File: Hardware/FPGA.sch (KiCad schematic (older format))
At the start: 6 parts, among them U501 W25Q128JVxxM, U502 ICE40UP5K-SG48, U503 Crystal Oscillator, U504 USBLC6-2

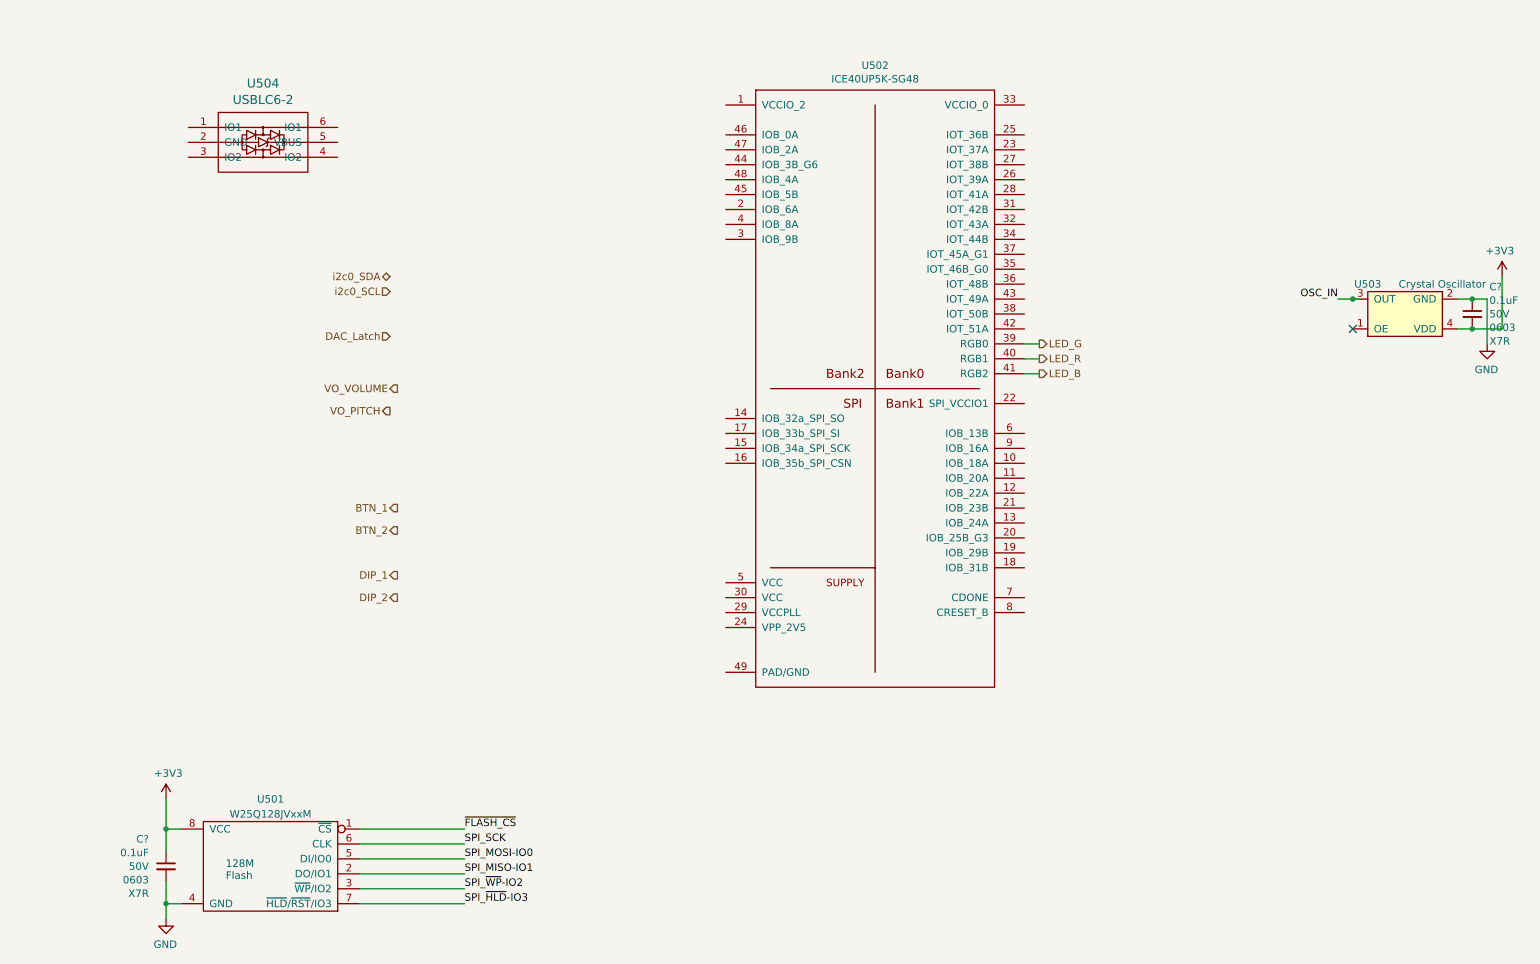
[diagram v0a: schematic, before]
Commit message: Putting in some connectivity. More passives.
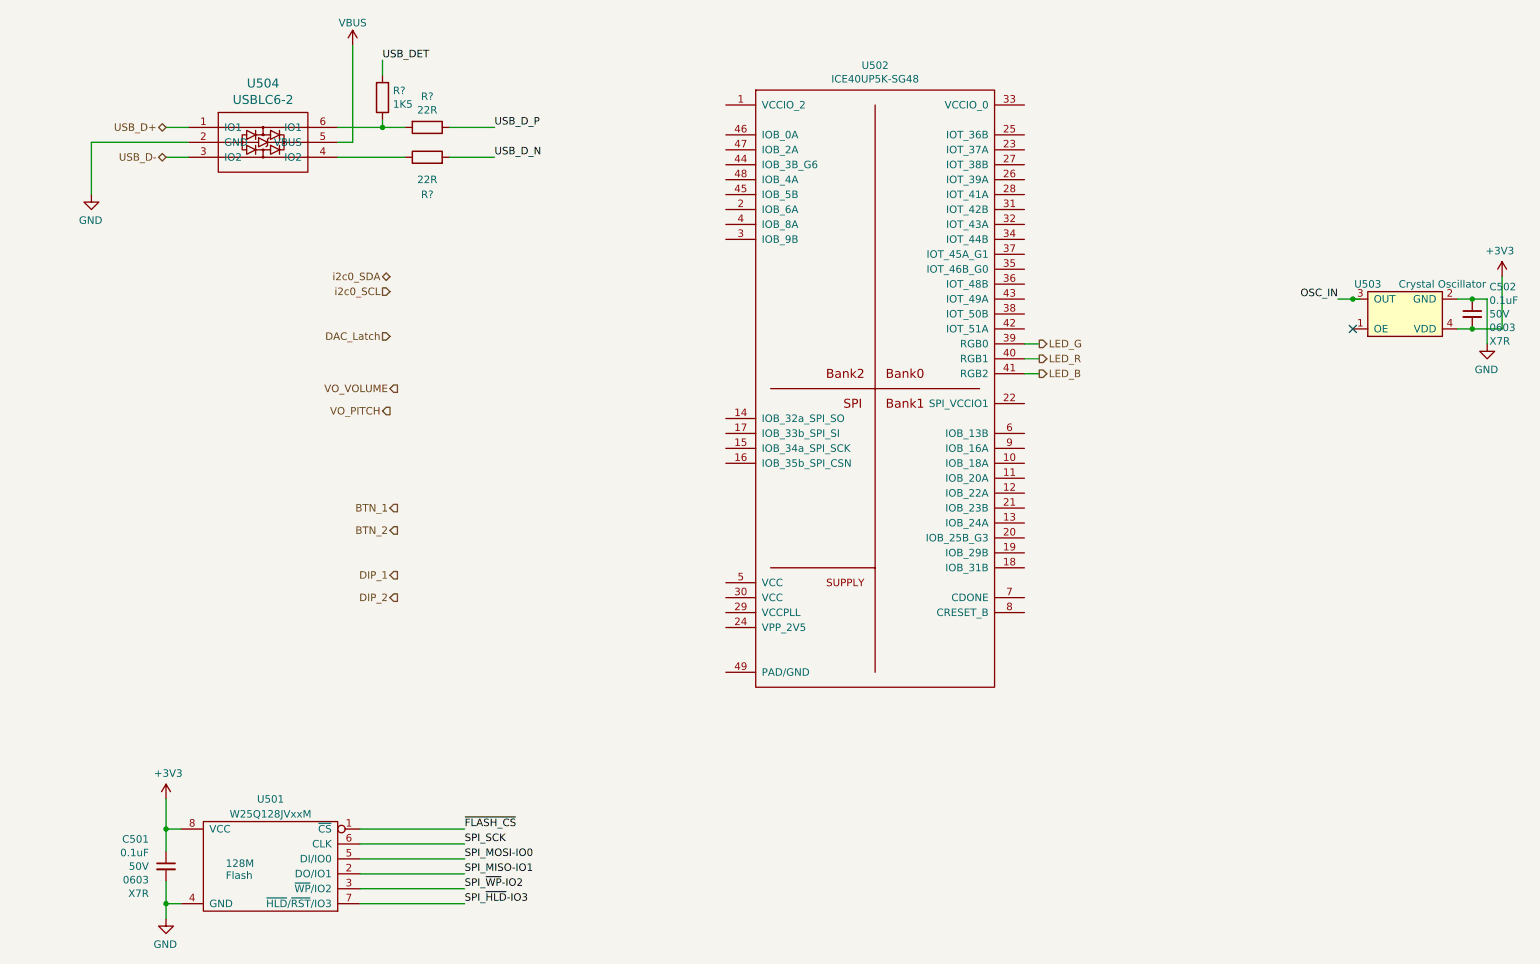
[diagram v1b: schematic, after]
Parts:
- added R? (x2): 22R, Resistor_SMD:R_0603_1608Metric, symbol Device:R
- added R?: 1K5, Resistor_SMD:R_0603_1608Metric, symbol Device:R
- gave numbers to parts that had none: 2
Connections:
- net labels added: USB_D+, USB_D-, USB_DET, USB_D_N, USB_D_P, VBUS
- wire segments 23 -> 36
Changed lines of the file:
@@
 P 10450 2650
 AR Path="/611E335F/61350B96" Ref="C?"  Part="1"
-AR Path="/611E3335/61350B96" Ref="C?"  Part="1"
-F 0 "C?" H 10565 2832 50  0000 L CNN
+AR Path="/611E3335/61350B96" Ref="C502"  Part="1"
+F 0 "C502" H 10565 2832 50  0000 L CNN
 F 1 "0.1uF" H 10565 2741 50  0000 L CNN
 F 2 "Capacitor_SMD:C_0603_1608Metric" H 10488 2500 50  0001 C CNN
@@
 	10450 2750 10650 2750
 $Comp
-L power:GND #PWR?
+L power:GND #PWR0108
 U 1 1 613565CE
 P 1700 6700
-F 0 "#PWR?" H 1700 6450 50  0001 C CNN
+F 0 "#PWR0108" H 1700 6450 50  0001 C CNN
 F 1 "GND" H 1705 6527 50  0000 C CNN
 F 2 "" H 1700 6700 50  0001 C CNN
@@
 	1700 5900 1700 6100
 $Comp
-L power:+3V3 #PWR?
+L power:+3V3 #PWR0109
 U 1 1 6135A9D4
 P 1700 5900
-F 0 "#PWR?" H 1700 5750 50  0001 C CNN
+F 0 "#PWR0109" H 1700 5750 50  0001 C CNN
 F 1 "+3V3" H 1715 6073 50  0000 C CNN
 F 2 "" H 1700 5900 50  0001 C CNN
@@
 P 1700 6350
 AR Path="/611E335F/6135A9DF" Ref="C?"  Part="1"
-AR Path="/611E3335/6135A9DF" Ref="C?"  Part="1"
-F 0 "C?" H 1815 6532 50  0000 L CNN
+AR Path="/611E3335/6135A9DF" Ref="C501"  Part="1"
+F 0 "C501" H 1815 6532 50  0000 L CNN
 F 1 "0.1uF" H 1815 6441 50  0000 L CNN
 F 2 "Capacitor_SMD:C_0603_1608Metric" H 1738 6200 50  0001 C CNN
@@
 Wire Wire Line
 	1700 6600 1800 6600
+$Comp
+L Device:R R?
+U 1 1 61492D03
+P 3450 1400
+AR Path="/61492D03" Ref="R?"  Part="1"
+AR Path="/611E3335/61492D03" Ref="R?"  Part="1"
+F 0 "R?" V 3243 1400 50  0000 C CNN
+F 1 "22R" V 3334 1400 50  0000 C CNN
+F 2 "Resistor_SMD:R_0603_1608Metric" V 3380 1400 50  0001 C CNN
+F 3 "~" H 3450 1400 50  0001 C CNN
+F 4 "CRGCQ0603J22R" V 3450 1400 50  0001 C CNN "MPN"
+F 5 "A130081CT-ND" V 3450 1400 50  0001 C CNN "DPN"
+	1    3450 1400
+	0    1    1    0
+$EndComp
+$Comp
+L Device:R R?
+U 1 1 61492D0B
+P 3150 1200
+AR Path="/61492D0B" Ref="R?"  Part="1"
+AR Path="/611E3335/61492D0B" Ref="R?"  Part="1"
+F 0 "R?" H 3080 1154 50  0000 R CNN
+F 1 "1K5" H 3080 1245 50  0000 R CNN
+F 2 "Resistor_SMD:R_0603_1608Metric" V 3080 1200 50  0001 C CNN
+F 3 "~" H 3150 1200 50  0001 C CNN
+F 4 "CRGCQ0603J1K5" V 3150 1200 50  0001 C CNN "MPN"
+F 5 "A130092CT-ND" V 3150 1200 50  0001 C CNN "DPN"
+	1    3150 1200
+	-1   0    0    1
+$EndComp
+$Comp
+L Device:R R?
+U 1 1 61492D13
+P 3450 1600
+AR Path="/61492D13" Ref="R?"  Part="1"
+AR Path="/611E3335/61492D13" Ref="R?"  Part="1"
+F 0 "R?" V 3200 1600 50  0000 C CNN
+F 1 "22R" V 3300 1600 50  0000 C CNN
+F 2 "Resistor_SMD:R_0603_1608Metric" V 3380 1600 50  0001 C CNN
+F 3 "~" H 3450 1600 50  0001 C CNN
+F 4 "CRGCQ0603J22R" V 3450 1600 50  0001 C CNN "MPN"
+F 5 "A130081CT-ND" V 3450 1600 50  0001 C CNN "DPN"
+	1    3450 1600
+	0    -1   -1   0
+$EndComp
+Text HLabel 1700 1400 0    50   BiDi ~ 0
+USB_D+
+Text HLabel 1700 1600 0    50   BiDi ~ 0
+USB_D-
+Text Label 3150 950  0    50   ~ 0
+USB_DET
+Wire Wire Line
+	3900 1400 3600 1400
+Wire Wire Line
+	3150 950  3150 1050
+Wire Wire Line
+	3150 1350 3150 1400
+Connection ~ 3150 1400
+Wire Wire Line
+	3150 1400 3300 1400
+Wire Wire Line
+	2850 1400 3150 1400
+$Comp
+L power:VBUS #PWR?
+U 1 1 614D3815
+P 2950 850
+AR Path="/61291C71/614D3815" Ref="#PWR?"  Part="1"
+AR Path="/614D3815" Ref="#PWR?"  Part="1"
+AR Path="/611E3335/614D3815" Ref="#PWR?"  Part="1"
+F 0 "#PWR?" H 2950 700 50  0001 C CNN
+F 1 "VBUS" H 2950 1000 50  0000 C CNN
+F 2 "" H 2950 850 50  0001 C CNN
+F 3 "" H 2950 850 50  0001 C CNN
+	1    2950 850
+	1    0    0    -1
+$EndComp
+Wire Wire Line
+	2950 850  2950 1500
+Wire Wire Line
+	2950 1500 2850 1500
+$Comp
+L power:GND #PWR?
+U 1 1 614D57CF
+P 1200 1850
+F 0 "#PWR?" H 1200 1600 50  0001 C CNN
+F 1 "GND" H 1205 1677 50  0000 C CNN
+F 2 "" H 1200 1850 50  0001 C CNN
+F 3 "" H 1200 1850 50  0001 C CNN
+	1    1200 1850
+	-1   0    0    -1
+$EndComp
+Wire Wire Line
+	1850 1500 1200 1500
+Wire Wire Line
+	1200 1500 1200 1850
+Wire Wire Line
+	1700 1400 1850 1400
+Wire Wire Line
+	1700 1600 1850 1600
+Wire Wire Line
+	2850 1600 3300 1600
+Wire Wire Line
+	3600 1600 3900 1600
+Text Label 3900 1400 0    50   ~ 0
+USB_D_P
+Text Label 3900 1600 0    50   ~ 0
+USB_D_N
 $EndSCHEMATC

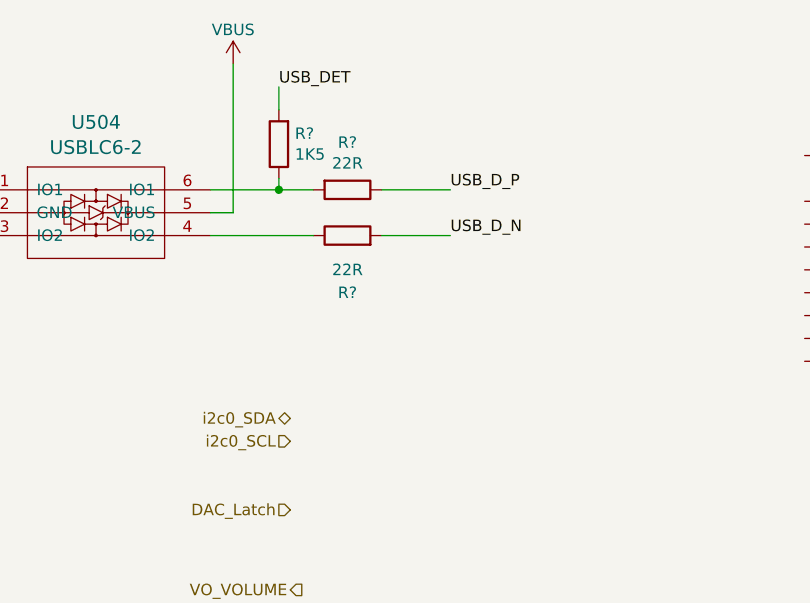
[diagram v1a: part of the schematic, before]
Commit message: More passives.
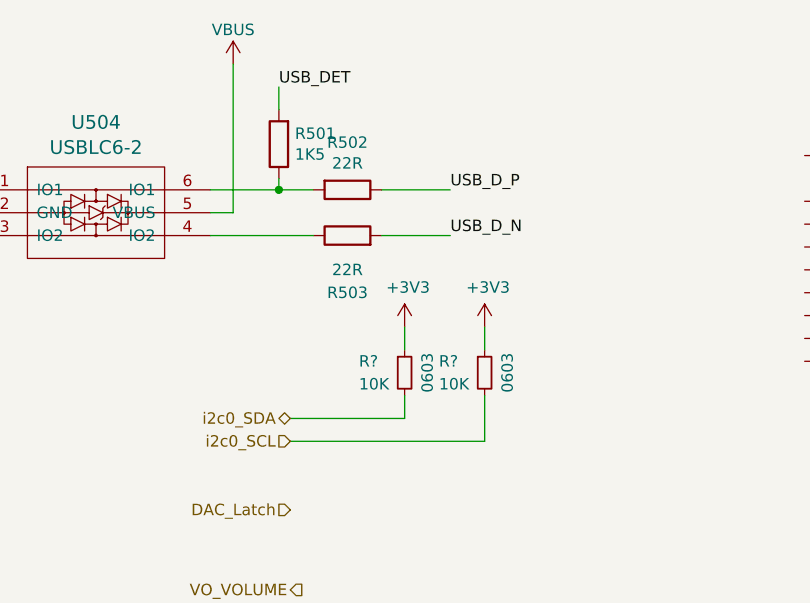
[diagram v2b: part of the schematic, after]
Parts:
- added R? (x2): 10K, Resistor_SMD:R_0603_1608Metric, symbol Device:R_Small
- gave numbers to parts that had none: 3
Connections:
- net +3V3: now also R?.1, R?.1
- net i2c0_SCL: now also R?.2
- net i2c0_SDA: now also R?.2
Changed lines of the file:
@@
 P 3450 1400
 AR Path="/61492D03" Ref="R?"  Part="1"
-AR Path="/611E3335/61492D03" Ref="R?"  Part="1"
-F 0 "R?" V 3243 1400 50  0000 C CNN
+AR Path="/611E3335/61492D03" Ref="R502"  Part="1"
+F 0 "R502" V 3243 1400 50  0000 C CNN
 F 1 "22R" V 3334 1400 50  0000 C CNN
 F 2 "Resistor_SMD:R_0603_1608Metric" V 3380 1400 50  0001 C CNN
@@
 P 3150 1200
 AR Path="/61492D0B" Ref="R?"  Part="1"
-AR Path="/611E3335/61492D0B" Ref="R?"  Part="1"
-F 0 "R?" H 3080 1154 50  0000 R CNN
+AR Path="/611E3335/61492D0B" Ref="R501"  Part="1"
+F 0 "R501" H 3080 1154 50  0000 R CNN
 F 1 "1K5" H 3080 1245 50  0000 R CNN
 F 2 "Resistor_SMD:R_0603_1608Metric" V 3080 1200 50  0001 C CNN
@@
 P 3450 1600
 AR Path="/61492D13" Ref="R?"  Part="1"
-AR Path="/611E3335/61492D13" Ref="R?"  Part="1"
-F 0 "R?" V 3200 1600 50  0000 C CNN
+AR Path="/611E3335/61492D13" Ref="R503"  Part="1"
+F 0 "R503" V 3200 1600 50  0000 C CNN
 F 1 "22R" V 3300 1600 50  0000 C CNN
 F 2 "Resistor_SMD:R_0603_1608Metric" V 3380 1600 50  0001 C CNN
@@
 AR Path="/61291C71/614D3815" Ref="#PWR?"  Part="1"
 AR Path="/614D3815" Ref="#PWR?"  Part="1"
-AR Path="/611E3335/614D3815" Ref="#PWR?"  Part="1"
-F 0 "#PWR?" H 2950 700 50  0001 C CNN
+AR Path="/611E3335/614D3815" Ref="#PWR0129"  Part="1"
+F 0 "#PWR0129" H 2950 700 50  0001 C CNN
 F 1 "VBUS" H 2950 1000 50  0000 C CNN
 F 2 "" H 2950 850 50  0001 C CNN
@@
 	2950 1500 2850 1500
 $Comp
-L power:GND #PWR?
+L power:GND #PWR0130
 U 1 1 614D57CF
 P 1200 1850
-F 0 "#PWR?" H 1200 1600 50  0001 C CNN
+F 0 "#PWR0130" H 1200 1600 50  0001 C CNN
 F 1 "GND" H 1205 1677 50  0000 C CNN
 F 2 "" H 1200 1850 50  0001 C CNN
@@
 Text Label 3900 1600 0    50   ~ 0
 USB_D_N
+$Comp
+L Device:R_Small R?
+U 1 1 61550D45
+P 3700 2200
+AR Path="/611E335F/61550D45" Ref="R?"  Part="1"
+AR Path="/61550D45" Ref="R?"  Part="1"
+AR Path="/611E3335/61550D45" Ref="R?"  Part="1"
+F 0 "R?" H 3500 2250 50  0000 L CNN
+F 1 "10K" H 3500 2150 50  0000 L CNN
+F 2 "Resistor_SMD:R_0603_1608Metric" V 3630 2200 50  0001 C CNN
+F 3 "~" H 3700 2200 50  0001 C CNN
+F 4 "0603" V 3800 2200 50  0000 C CNN "Pkg"
+F 5 "RNCP0603FTD10K0" H 3700 2200 50  0001 C CNN "MPN"
+F 6 "RNCP0603FTD10K0CT-ND" H 3700 2200 50  0001 C CNN "DPN"
+	1    3700 2200
+	1    0    0    -1
+$EndComp
+$Comp
+L Device:R_Small R?
+U 1 1 6155177C
+P 4050 2200
+AR Path="/611E335F/6155177C" Ref="R?"  Part="1"
+AR Path="/6155177C" Ref="R?"  Part="1"
+AR Path="/611E3335/6155177C" Ref="R?"  Part="1"
+F 0 "R?" H 3850 2250 50  0000 L CNN
+F 1 "10K" H 3850 2150 50  0000 L CNN
+F 2 "Resistor_SMD:R_0603_1608Metric" V 3980 2200 50  0001 C CNN
+F 3 "~" H 4050 2200 50  0001 C CNN
+F 4 "0603" V 4150 2200 50  0000 C CNN "Pkg"
+F 5 "RNCP0603FTD10K0" H 4050 2200 50  0001 C CNN "MPN"
+F 6 "RNCP0603FTD10K0CT-ND" H 4050 2200 50  0001 C CNN "DPN"
+	1    4050 2200
+	1    0    0    -1
+$EndComp
+$Comp
+L power:+3V3 #PWR?
+U 1 1 61554096
+P 3700 2000
+F 0 "#PWR?" H 3700 1850 50  0001 C CNN
+F 1 "+3V3" H 3715 2173 50  0000 C CNN
+F 2 "" H 3700 2000 50  0001 C CNN
+F 3 "" H 3700 2000 50  0001 C CNN
+	1    3700 2000
+	1    0    0    -1
+$EndComp
+$Comp
+L power:+3V3 #PWR?
+U 1 1 615544FD
+P 4050 2000
+F 0 "#PWR?" H 4050 1850 50  0001 C CNN
+F 1 "+3V3" H 4065 2173 50  0000 C CNN
+F 2 "" H 4050 2000 50  0001 C CNN
+F 3 "" H 4050 2000 50  0001 C CNN
+	1    4050 2000
+	1    0    0    -1
+$EndComp
+Wire Wire Line
+	3700 2000 3700 2100
+Wire Wire Line
+	4050 2000 4050 2100
+Wire Wire Line
+	3700 2300 3700 2400
+Wire Wire Line
+	3700 2400 3200 2400
+Wire Wire Line
+	4050 2300 4050 2500
+Wire Wire Line
+	4050 2500 3200 2500
 $EndSCHEMATC

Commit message: Option for tri-color reverse mount LED.
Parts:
- added R506, R507: DNF, Resistor_SMD:R_0402_1005Metric, symbol Device:R_Small
- gave numbers to parts that had none: 2
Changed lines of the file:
@@
 	1    0    0    -1
 $EndComp
-Text HLabel 3250 4100 0    50   Output ~ 0
+Text HLabel 1300 4250 0    50   Output ~ 0
 BTN_2
-Text HLabel 3250 3950 0    50   Output ~ 0
+Text HLabel 1300 4100 0    50   Output ~ 0
 BTN_1
-Text HLabel 3250 4550 0    50   Output ~ 0
+Text HLabel 1300 4700 0    50   Output ~ 0
 DIP_2
-Text HLabel 3250 4400 0    50   Output ~ 0
+Text HLabel 1300 4550 0    50   Output ~ 0
 DIP_1
 Wire Wire Line
@@
 AR Path="/611E335F/61550D45" Ref="R?"  Part="1"
 AR Path="/61550D45" Ref="R?"  Part="1"
-AR Path="/611E3335/61550D45" Ref="R?"  Part="1"
-F 0 "R?" H 3500 2250 50  0000 L CNN
+AR Path="/611E3335/61550D45" Ref="R504"  Part="1"
+F 0 "R504" H 3500 2250 50  0000 L CNN
 F 1 "10K" H 3500 2150 50  0000 L CNN
 F 2 "Resistor_SMD:R_0603_1608Metric" V 3630 2200 50  0001 C CNN
@@
 AR Path="/611E335F/6155177C" Ref="R?"  Part="1"
 AR Path="/6155177C" Ref="R?"  Part="1"
-AR Path="/611E3335/6155177C" Ref="R?"  Part="1"
-F 0 "R?" H 3850 2250 50  0000 L CNN
+AR Path="/611E3335/6155177C" Ref="R505"  Part="1"
+F 0 "R505" H 3850 2250 50  0000 L CNN
 F 1 "10K" H 3850 2150 50  0000 L CNN
 F 2 "Resistor_SMD:R_0603_1608Metric" V 3980 2200 50  0001 C CNN
@@
 $EndComp
 $Comp
-L power:+3V3 #PWR?
+L power:+3V3 #PWR0141
 U 1 1 61554096
 P 3700 2000
-F 0 "#PWR?" H 3700 1850 50  0001 C CNN
+F 0 "#PWR0141" H 3700 1850 50  0001 C CNN
 F 1 "+3V3" H 3715 2173 50  0000 C CNN
 F 2 "" H 3700 2000 50  0001 C CNN
@@
 $EndComp
 $Comp
-L power:+3V3 #PWR?
+L power:+3V3 #PWR0142
 U 1 1 615544FD
 P 4050 2000
-F 0 "#PWR?" H 4050 1850 50  0001 C CNN
+F 0 "#PWR0142" H 4050 1850 50  0001 C CNN
 F 1 "+3V3" H 4065 2173 50  0000 C CNN
 F 2 "" H 4050 2000 50  0001 C CNN
@@
 Wire Wire Line
 	4050 2500 3200 2500
+Text Label 1400 4550 0    50   ~ 0
+DIP_1
+Text Label 1400 4700 0    50   ~ 0
+DIP_2
+Text Label 1400 4100 0    50   ~ 0
+BTN_1
+Text Label 1400 4250 0    50   ~ 0
+BTN_2
+$Comp
+L Device:R_Small R?
+U 1 1 615CF009
+P 8000 5050
+AR Path="/611E335F/615CF009" Ref="R?"  Part="1"
+AR Path="/615CF009" Ref="R?"  Part="1"
+AR Path="/611E3335/615CF009" Ref="R506"  Part="1"
+F 0 "R506" H 8059 5096 50  0000 L CNN
+F 1 "DNF" H 8059 5005 50  0000 L CNN
+F 2 "Resistor_SMD:R_0402_1005Metric" V 7930 5050 50  0001 C CNN
+F 3 "~" H 8000 5050 50  0001 C CNN
+F 4 "0402" H 8150 5200 50  0000 C CNN "Pkg"
+F 5 "" H 8000 5050 50  0001 C CNN "MPN"
+F 6 "" H 8000 5050 50  0001 C CNN "DPN"
+	1    8000 5050
+	1    0    0    -1
+$EndComp
+$Comp
+L Device:R_Small R?
+U 1 1 615D7F58
+P 9800 4150
+AR Path="/611E335F/615D7F58" Ref="R?"  Part="1"
+AR Path="/615D7F58" Ref="R?"  Part="1"
+AR Path="/611E3335/615D7F58" Ref="R507"  Part="1"
+F 0 "R507" V 9900 3950 50  0000 L CNN
+F 1 "DNF" V 9700 4050 50  0000 L CNN
+F 2 "Resistor_SMD:R_0402_1005Metric" V 9730 4150 50  0001 C CNN
+F 3 "~" H 9800 4150 50  0001 C CNN
+F 4 "0402" V 9900 4250 50  0000 C CNN "Pkg"
+F 5 "" H 9800 4150 50  0001 C CNN "MPN"
+F 6 "" H 9800 4150 50  0001 C CNN "DPN"
+	1    9800 4150
+	0    1    1    0
+$EndComp
 $EndSCHEMATC

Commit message: Level shifting for DAC, some connectivity.
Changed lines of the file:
@@
 Text HLabel 3200 2400 0    50   BiDi ~ 0
 i2c0_SDA
-Text HLabel 3200 2500 0    50   Input ~ 0
+Text HLabel 3200 2500 0    50   Output ~ 0
 i2c0_SCL
-Text HLabel 3200 2800 0    50   Input ~ 0
+Text HLabel 3200 2800 0    50   Output ~ 0
 DAC_Latch
 Text HLabel 3250 3150 0    50   Output ~ 0
@@
 	1    0    0    -1
 $EndComp
-Text HLabel 1300 4250 0    50   Output ~ 0
+Text HLabel 1300 4250 0    50   Input ~ 0
 BTN_2
-Text HLabel 1300 4100 0    50   Output ~ 0
+Text HLabel 1300 4100 0    50   Input ~ 0
 BTN_1
-Text HLabel 1300 4700 0    50   Output ~ 0
+Text HLabel 1300 4700 0    50   Input ~ 0
 DIP_2
-Text HLabel 1300 4550 0    50   Output ~ 0
+Text HLabel 1300 4550 0    50   Input ~ 0
 DIP_1
 Wire Wire Line
@@
 	0    1    1    0
 $EndComp
+Text Label 8350 3700 0    50   ~ 0
+TRRS_Ring2_Switch
+Text Label 8350 3850 0    50   ~ 0
+TRRS_Sleeve_Switch
+Text Label 8350 4050 0    50   ~ 0
+TRRS_Sleeve_Switch
 $EndSCHEMATC
